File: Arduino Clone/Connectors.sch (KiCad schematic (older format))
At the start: 4 parts

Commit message: 30%
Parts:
- J1: renamed from J?; footprint (none) -> Connector_PinHeader_2.54mm:PinHeader_1x09_P2.54mm_Vertical
- J2: renamed from J?; footprint (none) -> Connector_PinHeader_2.54mm:PinHeader_2x03_P2.54mm_Vertical
- J3, J4: renamed from J?; footprint (none) -> Connector_PinHeader_2.54mm:PinHeader_1x04_P2.54mm_Vertical
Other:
- moved on the sheet: J1, J2, J3, J4
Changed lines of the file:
@@
 $EndDescr
 $Comp
-L Connector_Generic:Conn_01x09 J?
+L Connector_Generic:Conn_01x09 J1
 U 1 1 5FCF0074
-P 3850 3050
-F 0 "J?" H 3930 3092 50  0000 L CNN
-F 1 "Conn_01x09" H 3930 3001 50  0000 L CNN
-F 2 "" H 3850 3050 50  0001 C CNN
-F 3 "~" H 3850 3050 50  0001 C CNN
-	1    3850 3050
+P 4900 3200
+F 0 "J1" H 4980 3242 50  0000 L CNN
+F 1 "Conn_01x09" H 4980 3151 50  0000 L CNN
+F 2 "Connector_PinHeader_2.54mm:PinHeader_1x09_P2.54mm_Vertical" H 4900 3200 50  0001 C CNN
+F 3 "~" H 4900 3200 50  0001 C CNN
+	1    4900 3200
 	1    0    0    -1
 $EndComp
 $Comp
-L Connector_Generic:Conn_01x04 J?
+L Connector_Generic:Conn_01x04 J3
 U 1 1 5FCF0AC0
-P 5000 2850
-F 0 "J?" H 5080 2842 50  0000 L CNN
-F 1 "Conn_01x04" H 5080 2751 50  0000 L CNN
-F 2 "" H 5000 2850 50  0001 C CNN
-F 3 "~" H 5000 2850 50  0001 C CNN
-	1    5000 2850
+P 6350 3100
+F 0 "J3" H 6430 3092 50  0000 L CNN
+F 1 "Conn_01x04" H 6430 3001 50  0000 L CNN
+F 2 "Connector_PinHeader_2.54mm:PinHeader_1x04_P2.54mm_Vertical" H 6350 3100 50  0001 C CNN
+F 3 "~" H 6350 3100 50  0001 C CNN
+	1    6350 3100
 	1    0    0    -1
 $EndComp
 $Comp
-L Connector_Generic:Conn_02x03_Odd_Even J?
+L Connector_Generic:Conn_02x03_Odd_Even J2
 U 1 1 5FCF0EFC
-P 4900 3550
-F 0 "J?" H 4950 3867 50  0000 C CNN
-F 1 "Conn_02x03_Odd_Even" H 4950 3776 50  0000 C CNN
-F 2 "" H 4900 3550 50  0001 C CNN
-F 3 "~" H 4900 3550 50  0001 C CNN
-	1    4900 3550
+P 4900 4350
+F 0 "J2" H 4950 4667 50  0000 C CNN
+F 1 "Conn_02x03_Odd_Even" H 4950 4576 50  0000 C CNN
+F 2 "Connector_PinHeader_2.54mm:PinHeader_2x03_P2.54mm_Vertical" H 4900 4350 50  0001 C CNN
+F 3 "~" H 4900 4350 50  0001 C CNN
+	1    4900 4350
 	1    0    0    -1
 $EndComp
 $Comp
-L Connector_Generic:Conn_01x04 J?
+L Connector_Generic:Conn_01x04 J4
 U 1 1 5FCF1C90
-P 6100 2800
-F 0 "J?" H 6180 2792 50  0000 L CNN
-F 1 "Conn_01x04" H 6180 2701 50  0000 L CNN
-F 2 "" H 6100 2800 50  0001 C CNN
-F 3 "~" H 6100 2800 50  0001 C CNN
-	1    6100 2800
+P 6350 4300
+F 0 "J4" H 6430 4292 50  0000 L CNN
+F 1 "Conn_01x04" H 6430 4201 50  0000 L CNN
+F 2 "Connector_PinHeader_2.54mm:PinHeader_1x04_P2.54mm_Vertical" H 6350 4300 50  0001 C CNN
+F 3 "~" H 6350 4300 50  0001 C CNN
+	1    6350 4300
 	1    0    0    -1
 $EndComp

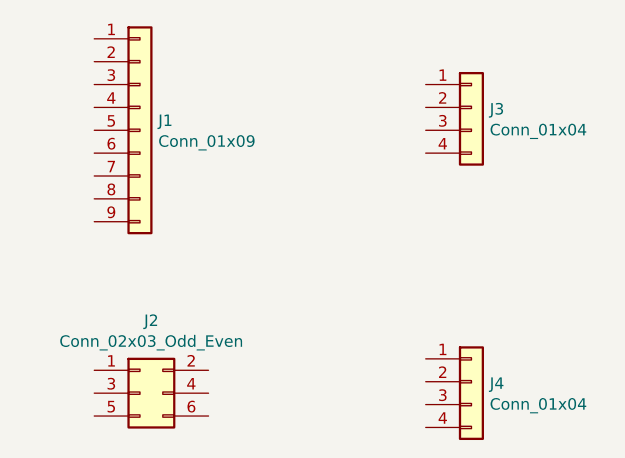
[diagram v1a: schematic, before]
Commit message: hierarchical label
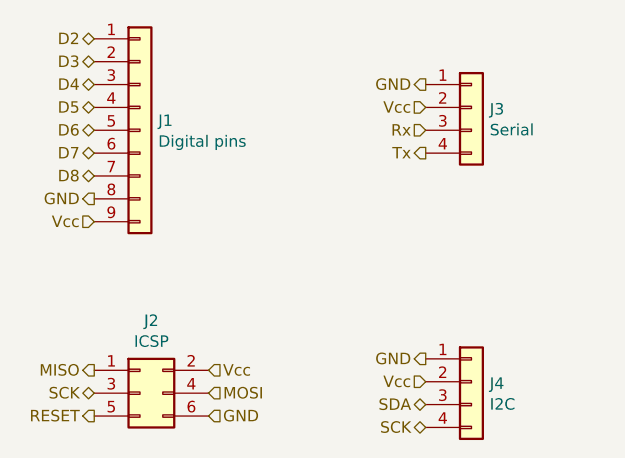
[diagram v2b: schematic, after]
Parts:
- J1: value Conn_01x09 -> Digital pins; footprint Connector_PinHeader_2.54mm:PinHeader_1x09_P2.54mm_Vertical -> Connector_PinSocket_2.54mm:PinSocket_1x09_P2.54mm_Vertical
- J2: value Conn_02x03_Odd_Even -> ICSP; footprint Connector_PinHeader_2.54mm:PinHeader_2x03_P2.54mm_Vertical -> Connector_PinSocket_2.54mm:PinSocket_2x03_P2.54mm_Vertical
- J3: value Conn_01x04 -> Serial; footprint Connector_PinHeader_2.54mm:PinHeader_1x04_P2.54mm_Vertical -> Connector_PinSocket_2.54mm:PinSocket_1x04_P2.54mm_Vertical
- J4: value Conn_01x04 -> I2C; footprint Connector_PinHeader_2.54mm:PinHeader_1x04_P2.54mm_Vertical -> Connector_PinSocket_2.54mm:PinSocket_1x04_P2.54mm_Vertical
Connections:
- net D2: now reaches J1.1 (Pin_1)
- net D3: now reaches J1.2 (Pin_2)
- net D4: now reaches J1.3 (Pin_3)
- net D5: now reaches J1.4 (Pin_4)
- net D6: now reaches J1.5 (Pin_5)
- net D7: now reaches J1.6 (Pin_6)
- net D8: now reaches J1.7 (Pin_7)
- net GND: now reaches J1.8 (Pin_8)
- net GND: now also J2.6 (Pin_6), J3.1 (Pin_1), J4.1 (Pin_1)
- net Vcc: now reaches J1.9 (Pin_9)
- net Vcc: now also J2.2 (Pin_2), J3.2 (Pin_2), J4.2 (Pin_2)
- net Rx: now reaches J3.3 (Pin_3)
- net Tx: now reaches J3.4 (Pin_4)
- net MISO: now reaches J2.1 (Pin_1)
- net SCK: now reaches J2.3 (Pin_3)
- net SCK: now also J4.4 (Pin_4)
- net MOSI: now reaches J2.4 (Pin_4)
- net RESET: now reaches J2.5 (Pin_5)
- net SDA: now reaches J4.3 (Pin_3)
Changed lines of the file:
@@
 P 4900 3200
 F 0 "J1" H 4980 3242 50  0000 L CNN
-F 1 "Conn_01x09" H 4980 3151 50  0000 L CNN
-F 2 "Connector_PinHeader_2.54mm:PinHeader_1x09_P2.54mm_Vertical" H 4900 3200 50  0001 C CNN
+F 1 " Digital pins" H 4980 3151 50  0000 L CNN
+F 2 "Connector_PinSocket_2.54mm:PinSocket_1x09_P2.54mm_Vertical" H 4900 3200 50  0001 C CNN
 F 3 "~" H 4900 3200 50  0001 C CNN
 	1    4900 3200
@@
 P 6350 3100
 F 0 "J3" H 6430 3092 50  0000 L CNN
-F 1 "Conn_01x04" H 6430 3001 50  0000 L CNN
-F 2 "Connector_PinHeader_2.54mm:PinHeader_1x04_P2.54mm_Vertical" H 6350 3100 50  0001 C CNN
+F 1 "Serial" H 6430 3001 50  0000 L CNN
+F 2 "Connector_PinSocket_2.54mm:PinSocket_1x04_P2.54mm_Vertical" H 6350 3100 50  0001 C CNN
 F 3 "~" H 6350 3100 50  0001 C CNN
 	1    6350 3100
@@
 P 4900 4350
 F 0 "J2" H 4950 4667 50  0000 C CNN
-F 1 "Conn_02x03_Odd_Even" H 4950 4576 50  0000 C CNN
-F 2 "Connector_PinHeader_2.54mm:PinHeader_2x03_P2.54mm_Vertical" H 4900 4350 50  0001 C CNN
+F 1 "ICSP" H 4950 4576 50  0000 C CNN
+F 2 "Connector_PinSocket_2.54mm:PinSocket_2x03_P2.54mm_Vertical" H 4900 4350 50  0001 C CNN
 F 3 "~" H 4900 4350 50  0001 C CNN
 	1    4900 4350
@@
 P 6350 4300
 F 0 "J4" H 6430 4292 50  0000 L CNN
-F 1 "Conn_01x04" H 6430 4201 50  0000 L CNN
-F 2 "Connector_PinHeader_2.54mm:PinHeader_1x04_P2.54mm_Vertical" H 6350 4300 50  0001 C CNN
+F 1 "I2C" H 6430 4201 50  0000 L CNN
+F 2 "Connector_PinSocket_2.54mm:PinSocket_1x04_P2.54mm_Vertical" H 6350 4300 50  0001 C CNN
 F 3 "~" H 6350 4300 50  0001 C CNN
 	1    6350 4300
 	1    0    0    -1
 $EndComp
+Text HLabel 4700 4250 0    50   Output ~ 0
+MISO
+Text HLabel 4700 4350 0    50   BiDi ~ 0
+SCK
+Text HLabel 4700 4450 0    50   Output ~ 0
+RESET
+Text HLabel 5200 4250 2    50   Input ~ 0
+Vcc
+Text HLabel 5200 4350 2    50   Input ~ 0
+MOSI
+Text HLabel 5200 4450 2    50   Input ~ 0
+GND
+Text HLabel 6150 3000 0    50   Output ~ 0
+GND
+Text HLabel 6150 3100 0    50   Input ~ 0
+Vcc
+Text HLabel 6150 3200 0    50   Input ~ 0
+Rx
+Text HLabel 6150 3300 0    50   Output ~ 0
+Tx
+Text HLabel 6150 4200 0    50   Output ~ 0
+GND
+Text HLabel 6150 4300 0    50   Input ~ 0
+Vcc
+Text HLabel 6150 4400 0    50   BiDi ~ 0
+SDA
+Text HLabel 6150 4500 0    50   BiDi ~ 0
+SCK
+Text HLabel 4700 2800 0    50   BiDi ~ 0
+D2
+Text HLabel 4700 2900 0    50   BiDi ~ 0
+D3
+Text HLabel 4700 3000 0    50   BiDi ~ 0
+D4
+Text HLabel 4700 3100 0    50   BiDi ~ 0
+D5
+Text HLabel 4700 3200 0    50   BiDi ~ 0
+D6
+Text HLabel 4700 3300 0    50   BiDi ~ 0
+D7
+Text HLabel 4700 3400 0    50   BiDi ~ 0
+D8
+Text HLabel 4700 3500 0    50   Output ~ 0
+GND
+Text HLabel 4700 3600 0    50   Input ~ 0
+Vcc
 $EndSCHEMATC

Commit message: labels
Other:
- note added: "GPIO Connector"
- note added: "I2C Connector"
- note added: "ICSP Connector"
- note added: "N1 - Connectors"
- note added: "Serial Connector"
- moved on the sheet: J2, J3, J4
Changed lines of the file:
@@
 L Connector_Generic:Conn_01x04 J3
 U 1 1 5FCF0AC0
-P 6350 3100
-F 0 "J3" H 6430 3092 50  0000 L CNN
-F 1 "Serial" H 6430 3001 50  0000 L CNN
-F 2 "Connector_PinSocket_2.54mm:PinSocket_1x04_P2.54mm_Vertical" H 6350 3100 50  0001 C CNN
-F 3 "~" H 6350 3100 50  0001 C CNN
-	1    6350 3100
+P 6400 2900
+F 0 "J3" H 6480 2892 50  0000 L CNN
+F 1 "Serial" H 6480 2801 50  0000 L CNN
+F 2 "Connector_PinSocket_2.54mm:PinSocket_1x04_P2.54mm_Vertical" H 6400 2900 50  0001 C CNN
+F 3 "~" H 6400 2900 50  0001 C CNN
+	1    6400 2900
 	1    0    0    -1
 $EndComp
@@
 L Connector_Generic:Conn_02x03_Odd_Even J2
 U 1 1 5FCF0EFC
-P 4900 4350
-F 0 "J2" H 4950 4667 50  0000 C CNN
-F 1 "ICSP" H 4950 4576 50  0000 C CNN
-F 2 "Connector_PinSocket_2.54mm:PinSocket_2x03_P2.54mm_Vertical" H 4900 4350 50  0001 C CNN
-F 3 "~" H 4900 4350 50  0001 C CNN
-	1    4900 4350
+P 4750 4550
+F 0 "J2" H 4800 4867 50  0000 C CNN
+F 1 "ICSP" H 4800 4776 50  0000 C CNN
+F 2 "Connector_PinSocket_2.54mm:PinSocket_2x03_P2.54mm_Vertical" H 4750 4550 50  0001 C CNN
+F 3 "~" H 4750 4550 50  0001 C CNN
+	1    4750 4550
 	1    0    0    -1
 $EndComp
@@
 L Connector_Generic:Conn_01x04 J4
 U 1 1 5FCF1C90
-P 6350 4300
-F 0 "J4" H 6430 4292 50  0000 L CNN
-F 1 "I2C" H 6430 4201 50  0000 L CNN
-F 2 "Connector_PinSocket_2.54mm:PinSocket_1x04_P2.54mm_Vertical" H 6350 4300 50  0001 C CNN
-F 3 "~" H 6350 4300 50  0001 C CNN
-	1    6350 4300
+P 6400 4500
+F 0 "J4" H 6480 4492 50  0000 L CNN
+F 1 "I2C" H 6480 4401 50  0000 L CNN
+F 2 "Connector_PinSocket_2.54mm:PinSocket_1x04_P2.54mm_Vertical" H 6400 4500 50  0001 C CNN
+F 3 "~" H 6400 4500 50  0001 C CNN
+	1    6400 4500
 	1    0    0    -1
 $EndComp
-Text HLabel 4700 4250 0    50   Output ~ 0
+Text HLabel 4550 4450 0    50   Output ~ 0
 MISO
-Text HLabel 4700 4350 0    50   BiDi ~ 0
+Text HLabel 4550 4550 0    50   BiDi ~ 0
 SCK
-Text HLabel 4700 4450 0    50   Output ~ 0
+Text HLabel 4550 4650 0    50   Output ~ 0
 RESET
-Text HLabel 5200 4250 2    50   Input ~ 0
+Text HLabel 5050 4450 2    50   Input ~ 0
 Vcc
-Text HLabel 5200 4350 2    50   Input ~ 0
+Text HLabel 5050 4550 2    50   Input ~ 0
 MOSI
-Text HLabel 5200 4450 2    50   Input ~ 0
+Text HLabel 5050 4650 2    50   Input ~ 0
 GND
-Text HLabel 6150 3000 0    50   Output ~ 0
+Text HLabel 6200 2800 0    50   Output ~ 0
 GND
-Text HLabel 6150 3100 0    50   Input ~ 0
+Text HLabel 6200 2900 0    50   Input ~ 0
 Vcc
-Text HLabel 6150 3200 0    50   Input ~ 0
+Text HLabel 6200 3000 0    50   Input ~ 0
 Rx
-Text HLabel 6150 3300 0    50   Output ~ 0
+Text HLabel 6200 3100 0    50   Output ~ 0
 Tx
-Text HLabel 6150 4200 0    50   Output ~ 0
+Text HLabel 6200 4400 0    50   Output ~ 0
 GND
-Text HLabel 6150 4300 0    50   Input ~ 0
+Text HLabel 6200 4500 0    50   Input ~ 0
 Vcc
-Text HLabel 6150 4400 0    50   BiDi ~ 0
+Text HLabel 6200 4600 0    50   BiDi ~ 0
 SDA
-Text HLabel 6150 4500 0    50   BiDi ~ 0
+Text HLabel 6200 4700 0    50   BiDi ~ 0
 SCK
 Text HLabel 4700 2800 0    50   BiDi ~ 0
@@
 Text HLabel 4700 3600 0    50   Input ~ 0
 Vcc
+Wire Notes Line
+	3300 1950 3300 5500
+Wire Notes Line
+	3300 5500 7850 5500
+Wire Notes Line
+	7850 5500 7850 1950
+Wire Notes Line
+	7850 1950 3300 1950
+Text Notes 5050 2650 2    50   ~ 0
+GPIO Connector
+Text Notes 6650 2650 2    50   ~ 0
+Serial Connector
+Text Notes 5050 4200 2    50   ~ 0
+ICSP Connector
+Text Notes 6600 4200 2    50   ~ 0
+I2C Connector
+Text Notes 3950 1900 2    50   ~ 0
+N1 - Connectors
 $EndSCHEMATC
